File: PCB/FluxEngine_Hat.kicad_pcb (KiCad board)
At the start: 2 copper layers, 83.8 x 24.1 mm, 6 parts, among them J1 Conn_01x26, J2 Conn_01x26, J3 Conn_01x03, J4 FDD_PC34_host, J5 FDD_Shugart50_host

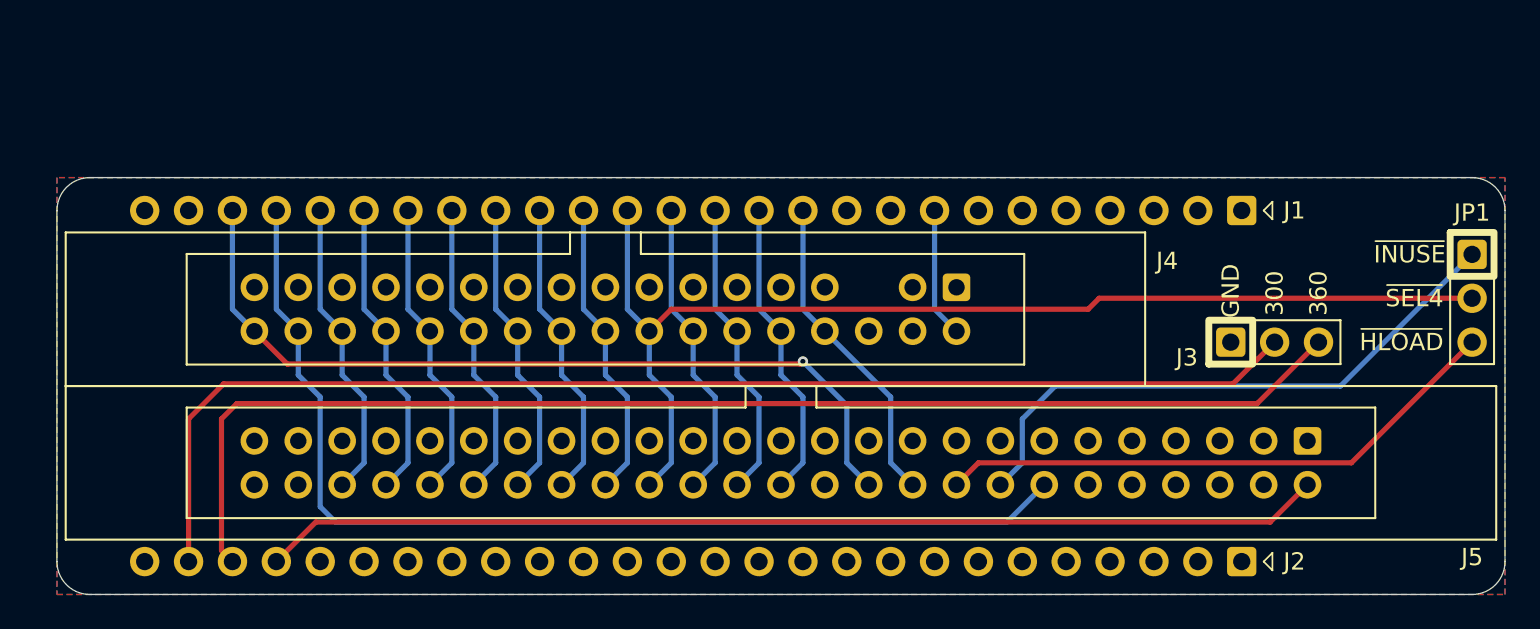
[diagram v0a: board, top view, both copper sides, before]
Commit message: v003 flip fpga board over
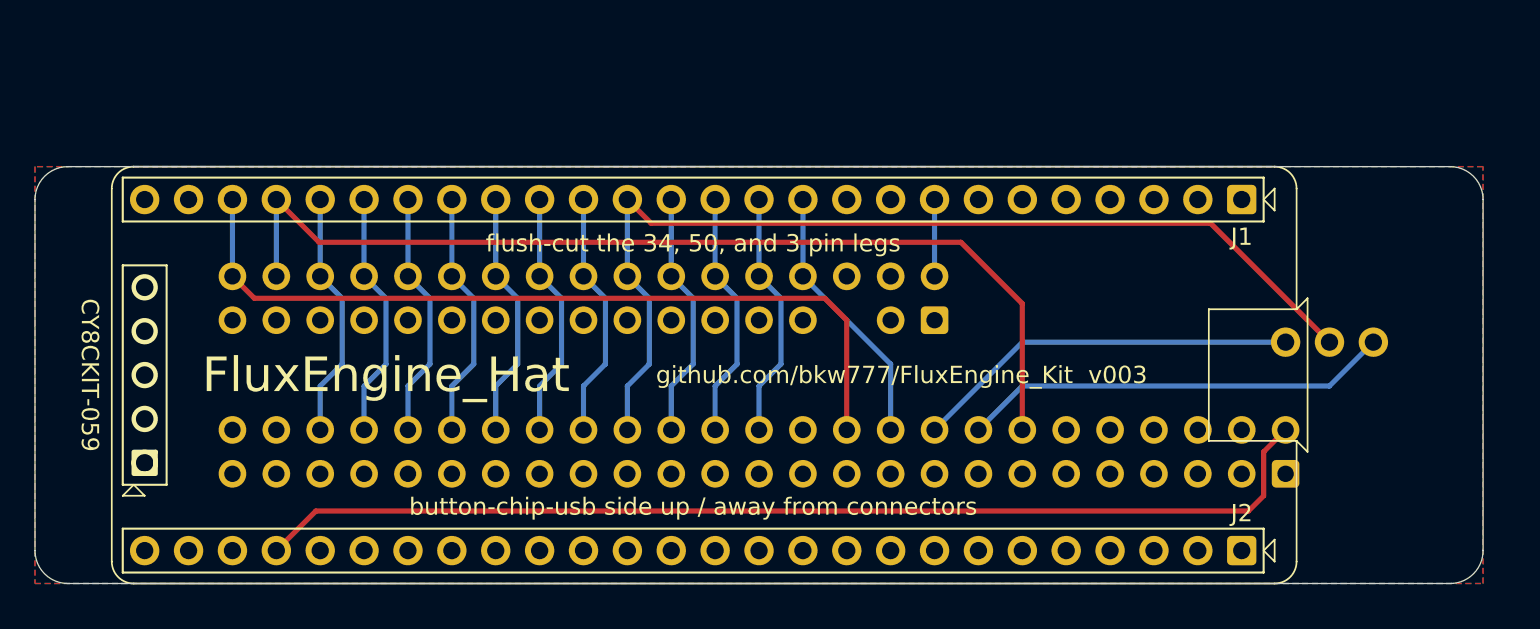
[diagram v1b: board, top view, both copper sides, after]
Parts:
- removed J2: Conn_01x26, 000_LOCAL:PinHeader_1x26_P2.54mm_Vertical
- removed J3: Conn_01x03, 000_LOCAL:PinHeader_1x03_P2.54mm_Vertical
- J1: value Conn_01x26 -> CY8CKIT-059; footprint 000_LOCAL:PinHeader_1x26_P2.54mm_Vertical -> 000_LOCAL:CY8CKIT-059; moved to F.Cu
- JP1: value Conn_01x03 -> Jumper_3_Open; footprint 000_LOCAL:PinHeader_1x03_P2.54mm_Vertical -> 000_LOCAL:PinHeader_1x03_P2.54mm_Vertical bare; moved to B.Cu
- P1: renamed from J4; value FDD_PC34_host -> FDD_IBMPC_host; moved to B.Cu
- P2: renamed from J5; value FDD_Shugart50_host -> FDD_SA800_host; moved to B.Cu
- moved JP1 7.65 mm to (179.1, 102.2), turned to 90 degrees
- moved P1 2.29 mm to (153.7, 101.0), turned to 90 degrees
- moved P2 2.29 mm to (174.0, 109.9), turned to 90 degrees
- moved J1 0.63 mm to (171.4, 94.0), turned to -90 degrees
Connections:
- P2 pad 10: /~{FD2S} -> unconnected-(J3-~{FD2S}-Pad10)
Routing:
- net /INDEX360: track 73.9 -> 0.00 mm
- net /INDEX300: track 73.0 -> 0.00 mm
- net /~{HLOAD}: track 33.3 -> 22.4 mm
- net /~{INUSE}: track 34.3 -> 25.0 mm
- net /~{SEL4}: track 65.9 -> 58.4 mm
- net /SIDE: track 61.4 -> 57.4 mm
- net /~{SEL3}: track 17.5 -> 14.4 mm
- net /WDATA: track 17.5 -> 14.4 mm
- net /~{WGATE}: track 17.5 -> 14.4 mm
- net /RDATA: track 17.5 -> 14.4 mm
- net /~{SEL1}: track 17.5 -> 14.4 mm
- net /~{INDEX}: track 18.5 -> 15.4 mm
- net /~{TRK0}: track 17.5 -> 14.4 mm
- net /~{WPROT}: track 17.5 -> 14.4 mm
- net /~{STEP}: track 17.5 -> 14.4 mm
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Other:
- board text added: "${COMMENT1} v${REVISION}"
- board text added: "${TITLE}"
- board text added: "3.5 INCH 5.25 INCH"
- board text added: "8 INCH"
- board text added: "FluxEngine"
- board text added: "button-chip-usb side up / away from connectors"
- board text added: "flush-cut the 34, 50, and 3 pin legs"
- board text removed: "${COMMENT1}"
- board text removed: "${TITLE} v${REVISION}"
- board text removed: "300"
- board text removed: "360"
- board text removed: "GND"
- board text removed: "J1"
- board text removed: "J2"
- board text removed: "RX"
- board text removed: "TX"
- board text removed: "VDD"
- board text removed: "VDDIO"
- board text removed: "pull pin 5 from 34-pin connector"
- board text removed: "~{SEL4}"

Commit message: jumper options and printable case
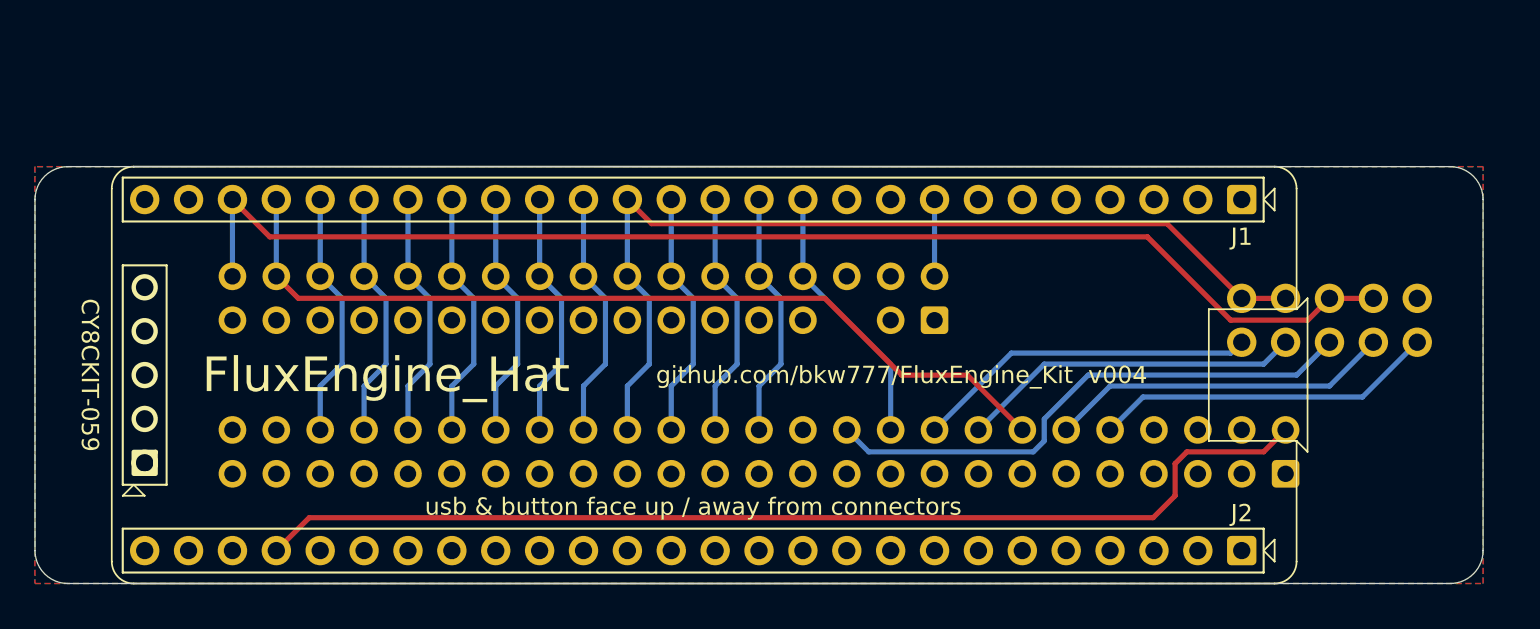
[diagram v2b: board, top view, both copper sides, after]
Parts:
- removed JP1: Jumper_3_Open, 000_LOCAL:PinHeader_1x03_P2.54mm_Vertical bare
- added J2: Conn_02x05_Odd_Even, 000_LOCAL:PinHeader_2x05_P2.54mm_Vertical, B.Cu at (181.6, 102.2)
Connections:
- net /TK43 renamed /TG43
- P2 pad 10: unconnected-(J3-~{FD2S}-Pad10) -> /~{FD2S}
- P2 pad 12: unconnected-(J3-DSKCHG-Pad12) -> /DC
- P2 pad 22: /~{READY} -> /~{RDY}
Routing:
- net /~{RDY}: track 0.00 -> 31.8 mm
- net /~{READY}: track 47.4 -> 73.9 mm
- net /~{FD2S}: track 0.00 -> 19.9 mm
- net /DC: track 0.00 -> 19.9 mm
- net /SIDE: track 57.4 -> 51.3 mm
- net /~{INUSE}: track 25.0 -> 19.9 mm
- net /~{SEL4}: track 58.4 -> 54.9 mm
- net /~{HLOAD}: track 22.4 -> 19.9 mm
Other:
- board text added: "FD2S DSKCH READY DLOCK HLD"
- board text added: "usb & button face up / away from connectors"
- board text removed: "button-chip-usb side up / away from connectors"
- board text removed: "flush-cut the 34, 50, and 3 pin legs"
- board text removed: "~{HLOAD}"
- board text removed: "~{INUSE}"

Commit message: snap cover, better 3d model files
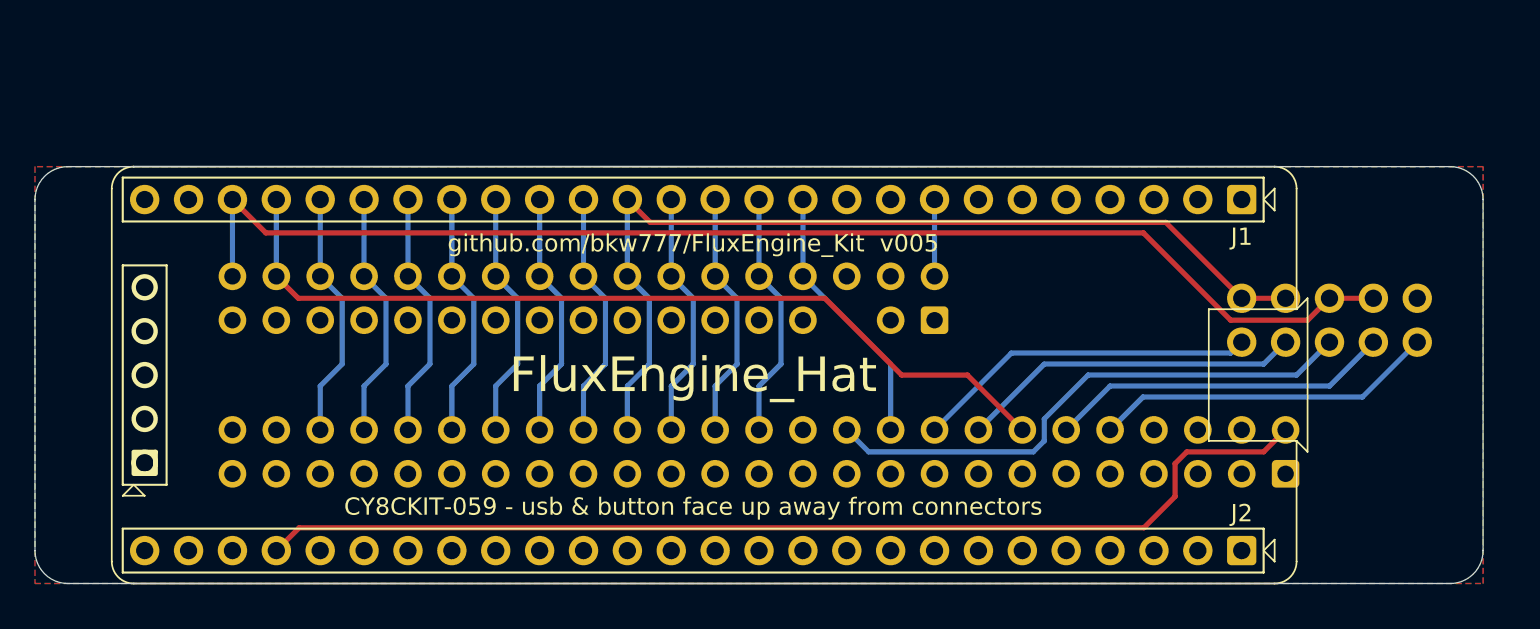
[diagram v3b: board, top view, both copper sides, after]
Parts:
- J1: value CY8CKIT-059 -> CY8CKIT-059 - usb & button face up away from connectors
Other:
- board text removed: "usb & button face up / away from connectors"

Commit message: delete type B, improve cover
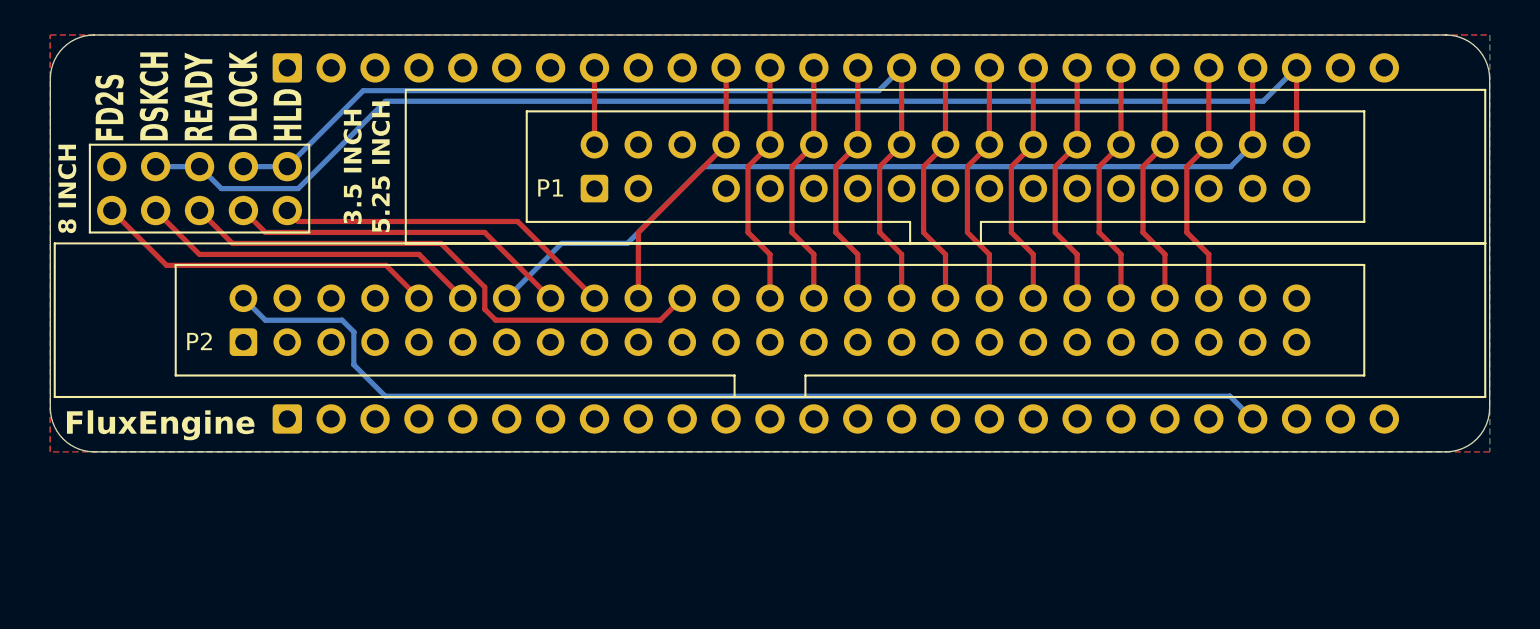
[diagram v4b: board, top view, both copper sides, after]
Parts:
- J1: value CY8CKIT-059 - usb & button face up away from connectors -> CY8CKIT-059 usb & button face away from hat; moved to B.Cu
- J2, P1, P2: moved to F.Cu
- moved J2 75.9 mm to (106.0, 94.6)
- moved P2 60.8 mm to (113.7, 102.2)
- moved J1 55.8 mm to (116.2, 86.4)
- moved P1 21.1 mm to (134.0, 93.3)
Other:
- board size 83.8 x 24.1 mm -> 83.3 x 24.1 mm
